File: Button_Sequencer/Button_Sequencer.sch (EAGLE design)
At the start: 85 parts, among them IC1 OPA2134P

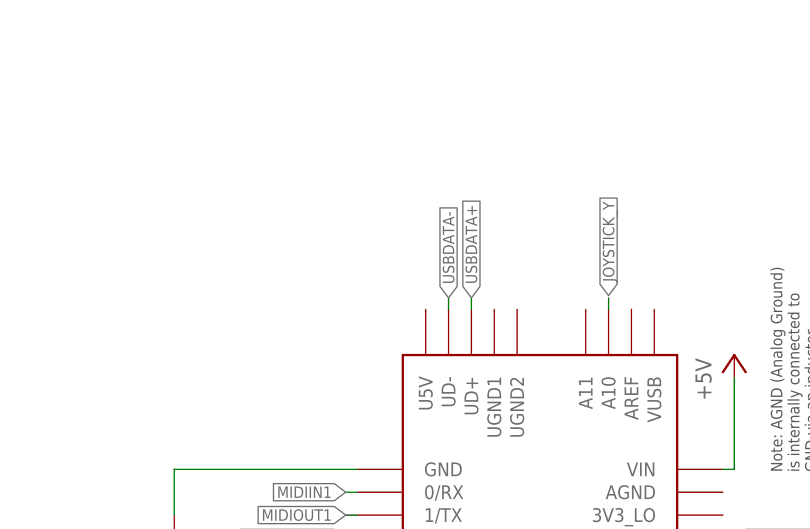
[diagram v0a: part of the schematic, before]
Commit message: Fixed lost commit from merger
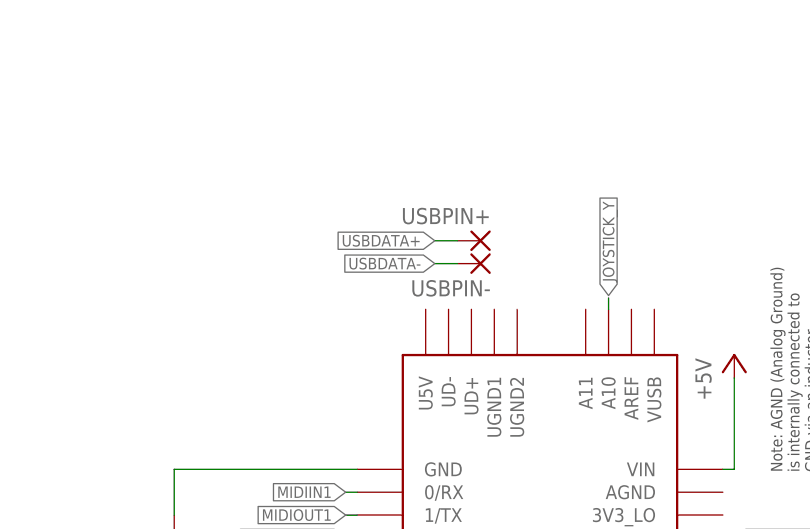
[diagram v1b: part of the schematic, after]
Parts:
- added USBPIN+, USBPIN-: (no value), wirepad:1,6/0,8
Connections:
- net USBDATA+: now also USBPIN+.P; no longer TEENSY_3.6.UD+
- net USBDATA-: now also USBPIN-.P; no longer TEENSY_3.6.UD-
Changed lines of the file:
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@@
 <part name="GND15" library="supply1" library_urn="urn:adsk.eagle:library:371" deviceset="GND" device=""/>
 <part name="GND16" library="supply1" library_urn="urn:adsk.eagle:library:371" deviceset="GND" device=""/>
+<part name="USBPIN+" library="wirepad" library_urn="urn:adsk.eagle:library:412" deviceset="1,6/0,8" device="" package3d_urn="urn:adsk.eagle:package:30830/1"/>
+<part name="USBPIN-" library="wirepad" library_urn="urn:adsk.eagle:library:412" deviceset="1,6/0,8" device="" package3d_urn="urn:adsk.eagle:package:30830/1"/>
 </parts>
 <sheets>
@@
 <instance part="GND16" gate="1" x="104.14" y="157.48" smashed="yes">
 <attribute name="VALUE" x="101.6" y="154.94" size="1.778" layer="96"/>
+</instance>
+<instance part="USBPIN+" gate="P" x="332.74" y="213.36" smashed="yes" rot="MR0">
+<attribute name="NAME" x="333.883" y="215.2142" size="1.778" layer="95" rot="MR0"/>
+<attribute name="VALUE" x="333.883" y="210.058" size="1.778" layer="96" rot="MR0"/>
+</instance>
+<instance part="USBPIN-" gate="P" x="332.74" y="210.82" smashed="yes" rot="R180">
+<attribute name="NAME" x="333.883" y="208.9658" size="1.778" layer="95" rot="R180"/>
+<attribute name="VALUE" x="333.883" y="214.122" size="1.778" layer="96" rot="R180"/>
 </instance>
 </instances>
@@
 </segment>
 <segment>
-<pinref part="TEENSY_3.6" gate="G$1" pin="UD+"/>
-<wire x1="331.724" y1="205.74" x2="331.724" y2="207.01" width="0.1524" layer="91"/>
-<label x="331.724" y="207.01" size="1.27" layer="95" rot="R90" xref="yes"/>
+<pinref part="USBPIN+" gate="P" pin="P"/>
+<wire x1="330.2" y1="213.36" x2="327.66" y2="213.36" width="0.1524" layer="91"/>
+<label x="327.66" y="213.36" size="1.27" layer="95" rot="R180" xref="yes"/>
 </segment>
 </net>
@@
 </segment>
 <segment>
-<pinref part="TEENSY_3.6" gate="G$1" pin="UD-"/>
-<wire x1="329.184" y1="205.74" x2="329.184" y2="207.01" width="0.1524" layer="91"/>
-<label x="329.184" y="207.01" size="1.27" layer="95" rot="R90" xref="yes"/>
-</segment>
-</net>
+<pinref part="USBPIN-" gate="P" pin="P"/>
+<wire x1="330.2" y1="210.82" x2="327.66" y2="210.82" width="0.1524" layer="91"/>
+<label x="327.66" y="210.82" size="1.27" layer="95" rot="R180" xref="yes"/>
+</segment>
+</net>

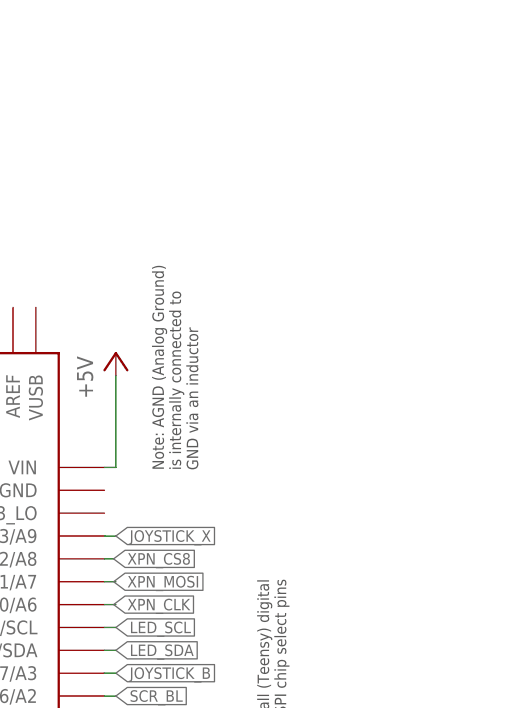
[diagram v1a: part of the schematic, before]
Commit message: Added +-12V barrel connetor TODO single +12V supply varient
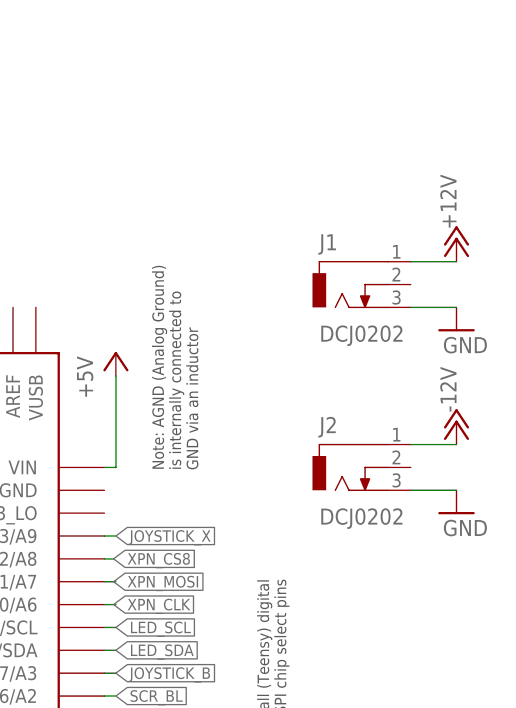
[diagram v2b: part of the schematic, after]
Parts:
- added J1, J2: DCJ0202, con-jack:DCJ0202
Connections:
- net +12V: now also J1.1
- net -12V: now also J2.1
- net GND: now also J1.3, J2.3
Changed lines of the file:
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@@
 <part name="USBPIN+" library="wirepad" library_urn="urn:adsk.eagle:library:412" deviceset="1,6/0,8" device="" package3d_urn="urn:adsk.eagle:package:30830/1"/>
 <part name="USBPIN-" library="wirepad" library_urn="urn:adsk.eagle:library:412" deviceset="1,6/0,8" device="" package3d_urn="urn:adsk.eagle:package:30830/1"/>
+<part name="J1" library="con-jack" library_urn="urn:adsk.eagle:library:154" deviceset="DCJ0202" device="" package3d_urn="urn:adsk.eagle:package:7491/1"/>
+<part name="J2" library="con-jack" library_urn="urn:adsk.eagle:library:154" deviceset="DCJ0202" device="" package3d_urn="urn:adsk.eagle:package:7491/1"/>
+<part name="P-3" library="supply1" library_urn="urn:adsk.eagle:library:371" deviceset="-12V" device=""/>
+<part name="P+3" library="supply1" library_urn="urn:adsk.eagle:library:371" deviceset="+12V" device=""/>
+<part name="GND17" library="supply1" library_urn="urn:adsk.eagle:library:371" deviceset="GND" device=""/>
+<part name="GND18" library="supply1" library_urn="urn:adsk.eagle:library:371" deviceset="GND" device=""/>
 </parts>
 <sheets>
@@
 <attribute name="NAME" x="333.883" y="208.9658" size="1.778" layer="95" rot="R180"/>
 <attribute name="VALUE" x="333.883" y="214.122" size="1.778" layer="96" rot="R180"/>
+</instance>
+<instance part="J1" gate="G$1" x="386.08" y="208.28" smashed="yes">
+<attribute name="NAME" x="383.54" y="212.09" size="1.778" layer="95"/>
+<attribute name="VALUE" x="383.54" y="201.93" size="1.778" layer="96"/>
+</instance>
+<instance part="J2" gate="G$1" x="386.08" y="187.96" smashed="yes">
+<attribute name="NAME" x="383.54" y="191.77" size="1.778" layer="95"/>
+<attribute name="VALUE" x="383.54" y="181.61" size="1.778" layer="96"/>
+</instance>
+<instance part="P-3" gate="1" x="398.78" y="193.04" smashed="yes" rot="R180">
+<attribute name="VALUE" x="398.78" y="194.056" size="1.778" layer="96" rot="R90"/>
+</instance>
+<instance part="P+3" gate="1" x="398.78" y="213.36" smashed="yes">
+<attribute name="VALUE" x="398.78" y="214.376" size="1.778" layer="96" rot="R90"/>
+</instance>
+<instance part="GND17" gate="1" x="398.78" y="182.88" smashed="yes">
+<attribute name="VALUE" x="397.256" y="180.34" size="1.778" layer="96"/>
+</instance>
+<instance part="GND18" gate="1" x="398.78" y="203.2" smashed="yes">
+<attribute name="VALUE" x="397.256" y="200.66" size="1.778" layer="96"/>
 </instance>
 </instances>
@@
 <pinref part="GND16" gate="1" pin="GND"/>
 </segment>
+<segment>
+<pinref part="GND17" gate="1" pin="GND"/>
+<pinref part="J2" gate="G$1" pin="3"/>
+<wire x1="398.78" y1="185.42" x2="393.7" y2="185.42" width="0.1524" layer="91"/>
+</segment>
+<segment>
+<pinref part="GND18" gate="1" pin="GND"/>
+<pinref part="J1" gate="G$1" pin="3"/>
+<wire x1="398.78" y1="205.74" x2="393.7" y2="205.74" width="0.1524" layer="91"/>
+</segment>
 </net>
 <net name="+3V3" class="0">
@@
 <wire x1="114.3" y1="167.894" x2="114.3" y2="162.56" width="0.1524" layer="91"/>
 <junction x="114.3" y="162.56"/>
+</segment>
+<segment>
+<pinref part="J1" gate="G$1" pin="1"/>
+<pinref part="P+3" gate="1" pin="+12V"/>
+<wire x1="398.78" y1="210.82" x2="393.7" y2="210.82" width="0.1524" layer="91"/>
 </segment>
 </net>
@@
 <junction x="78.74" y="162.56"/>
 </segment>
-</net>
+<segment>
+<pinref part="J2" gate="G$1" pin="1"/>
+<pinref part="P-3" gate="1" pin="-12V"/>
+<wire x1="398.78" y1="190.5" x2="393.7" y2="190.5" width="0.1524" layer="91"/>
+</segment>
+</net>
